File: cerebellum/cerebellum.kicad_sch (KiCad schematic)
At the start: 83 parts, among them J1 Power_IN, J10 Arm_R, J11 Light, J2 Power_Back, J3 GD_LINK, J4 GD_LINK, J5 Head, J7 Leg_L, J8 Leg_R, J9 Arm_L, Q1 AP2300, Q2 FH1404G6, Q3 FH1404G6, Q4 FH1404G6, U1 GD32F405VGHx, U2 TPS5430DDAR, U3 BMI088, U4 TCAN4550RGYRQ1, U5 ICP-20100, Y1 8M, Y2 40M

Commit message: [New] Complete new cerebellum
1. it's based on NXP MIMXRT1061CVL5A
2. it supports xt30(2+2)x7 output, xt60x1 input
3. it supports CAN FD & CAN 2.0

Signed-off-by: Homalozoa <nx.tardis@gmail.com>
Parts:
- removed J2: Power_Back, Rolling_Custom:AMASS_XT60PW-M, symbol Rolling_Custom:XT60PW-M
- removed L1: 20R, Resistor_SMD:R_0402_1005Metric, symbol Device:L_Ferrite
- removed Q2, Q3, Q4: FH1404G6, Rolling_Custom:PDFN5X6-8L, symbol Rolling_Custom:WNM6006
- removed U1: GD32F405VGHx, Rolling_Custom:Modified-BGA-100_7x7mm_Layout12x12_P0.5mm, symbol Rolling_Custom:GD32F405VGHx
- removed U4: TCAN4550RGYRQ1, Rolling_Custom:VQFN20, symbol Rolling_Custom:TCAN4550RGYRQ1
- removed Y1: 8M, Oscillator:Oscillator_SMD_EuroQuartz_XO32-4Pin_3.2x2.5mm, symbol Device:Crystal_GND24
- removed Y2: 40M, Oscillator:Oscillator_SMD_EuroQuartz_XO32-4Pin_3.2x2.5mm, symbol Device:Crystal_GND24
- added C36: 47uf 50V, Capacitor_SMD:C_0603_1608Metric, symbol Device:C
- added C38: 100nF, 10%, 10V, Capacitor_SMD:C_0402_1005Metric, symbol Device:C
- added D5: LTST-C281KFKT-5A, LED_SMD:LED_0402_1005Metric, symbol Device:LED
- added D6, D7: 12V, Diode_SMD:D_SOD-323, symbol Device:D_TVS
- added D8: B240, Diode_SMD:D_SMB, symbol Diode:B240
- added J12: Back, Rolling_Custom:XT30PW(2+2), symbol Rolling_Custom:XT30PW(2+2)
- added J2: UART, Connector_JST:JST_GH_SM03B-GHS-TB_1x03-1MP_P1.25mm_Horizontal, symbol Connector:Conn_01x03_Female
- added L1: 15uh, Inductor_SMD:L_0603_1608Metric, symbol Device:L
- added R16: 10.2k, Resistor_SMD:R_0402_1005Metric, symbol Device:R_US
- added R17: 1.96k, Resistor_SMD:R_0402_1005Metric, symbol Device:R_US
- added U1: OK1061-S, Rolling_Custom:OK1061-S-100, symbol Rolling_Custom:OK1061-S
- added U4, U6: TJA1042T, Package_SO:SOIC-8_3.9x4.9mm_P1.27mm, symbol Interface_CAN_LIN:TJA1042T
- added U7: TPS54231, Package_SO:SOIC-8_3.9x4.9mm_P1.27mm, symbol Regulator_Switching:TPS54233
- C1: value 20pF, 10%, 10V -> 100nF, 10%, 10V
- C11, C9: value 10uF, 10%, 10V -> 100pF, 10%, 10V
- C12, C8: value 100nF, 10%, 10V -> 4.7uF, 10%, 10V
- C14: value 8.2pF, 10%, 50V -> 10pf 50V
- C15: value 8.2pF, 10%, 50V -> 1.5nf 50V; footprint Capacitor_SMD:C_0402_1005Metric -> Capacitor_SMD:C_0603_1608Metric
- C16: value 10nF, 10%, 50V -> 4.7uF 50V; footprint Capacitor_SMD:C_0402_1005Metric -> Capacitor_SMD:C_0805_2012Metric
- C18: value 470nF, 10%, 50V -> 4.7uF 50V; footprint Capacitor_SMD:C_0603_1608Metric -> Capacitor_SMD:C_0805_2012Metric
- C25: value 100nF, 10%, 50V -> 10uf 50V
- C26: value 10uF, 10%, 50V -> 8.2nf 50V
- C27: value 10uF, 10%, 50V -> 100nF, 10%, 10V; footprint Capacitor_SMD:C_0603_1608Metric -> Capacitor_SMD:C_0402_1005Metric
- C3: value 20pF, 10%, 10V -> 4.7uF, 10%, 10V
- C33: value 10uF, 10%, 10V -> 47uf 50V; footprint Capacitor_SMD:C_0402_1005Metric -> Capacitor_SMD:C_0603_1608Metric
- C4: value 100nF, 10%, 10V -> 1uF, 10%, 10V
- C6: value 4.7uF, 10%, 10V -> 10uF, 10%, 10V
- C7: value 1uF, 10%, 10V -> 100nF, 10%, 10V
- D2: footprint Diode_SMD:D_SOD-523 -> Diode_SMD:D_SMC
- J3: value GD_LINK -> SWD_DBG
- J4: value GD_LINK -> SWD_DBG_PIN
- J6: value (none) -> CAN; footprint (none) -> Connector_JST:JST_GH_BM02B-GHS-TBT_1x02-1MP_P1.25mm_Vertical
- R1: value 10k, 5% -> 1k
- R2: value 10k, 5% -> 120R
- R3: value 0 -> 64.9k
- R4: value 33k -> 169k
- R5: value 3k -> 20.5
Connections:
- net ICP_SCK is gone; now on net SENSOR_SCK: U5.2 (SCL)
- net ICP_SDI is gone; now on net SENSOR_SDI: U5.4 (SDA/SDIO/SDI)
- net ICP_SDO is gone; now on net SENSOR_SDO: U5.6 (SDO/AD0)
- net MCU_OSC_IN is gone; now on net GND: C1.2
- net MCU_OSC_OUT is gone; now on net GND: C3.2
- net PWR_EXPORT is gone; now on net +24V: C34.1, C35.1, C37.1, C39.1, C41.1, J10.1 (VBUS), J11.1 (VBUS), J5.1 (VBUS), J7.1 (VBUS), J8.1 (VBUS), J9.1 (VBUS)
- net TCAN_OSC_IN is gone; now on net GND: C14.2
- net TCAN_OSC_OUT is gone; now on net GND: C15.2
- net TCAN_WAKE is gone; now on net +24V: R4.1
- net +24V: now also C16.1, C18.1, J12.1 (VBUS), U7.2 (VIN); no longer C26.1, R5.1
- net +3V3: now also R1.2; no longer C10.2, C33.1, C4.1, C5.1, C6.1, C7.1, C8.1, C9.2, J3.1 (Pin_1), R1.1
- net ACC_SCS: now also U1.46 (LPSPI1_PCS2)
- net BMI_HEAT: now also U1.72 (FLEXPWM1_PWMA2)
- net CAN_H: now also U4.7 (CANH); no longer J10.3 (CAN_H), J11.3 (CAN_H), J5.3 (CAN_H), J7.3 (CAN_H), J8.3 (CAN_H), J9.3 (CAN_H)
- net CAN_L: now also U4.6 (CANL); no longer J10.4 (CAN_L), J11.4 (CAN_L), J5.4 (CAN_L), J7.4 (CAN_L), J8.4 (CAN_L), J9.4 (CAN_L)
- net GND: now also C10.2, C11.1, C12.2, C16.2, R5.2, C36.2, C38.1, D6.2 (A2), D7.2 (A2), D8.2 (A), J2.3 (Pin_3), R17.2, U1.10 (GND), U1.25 (GND), U1.26 (GND), U1.3 (GND), U1.36 (GND), U1.4 (GND), U1.48 (BOOT_MODE0), U1.49 (BOOT_MODE1), U1.5 (GND), U1.50 (GND), U1.51 (GND), U1.52 (LCDIF_DATA06), U1.53 (LCDIF_DATA07), U1.67 (GND), U1.74 (GND), U1.75 (GND), U1.76 (GND), U1.82 (GND), U1.90 (GND), U4.2 (GND), U6.2 (GND), U7.7 (GND); no longer C1.1, C10.1, C14.1, C15.1, C16.1, C27.2, C3.1, R2.2, R3.1
- net GNDA: now also J12.2 (GND)
- net GYRO_SCS: now also U1.45 (LPSPI1_PCS3)
- net ICP_INT: now also U1.80 (GPIO3_IO00)
- net ICP_SCS: now also U1.70 (LPSPI1_PCS0)
- net SWCLK: now also U1.33 (SWCLK)
- net SWDIO: now also U1.32 (SWDIO)
- net CANFD_H: now reaches R2.1
- net CANFD_H: now also C11.2, J10.3 (CAN_H), J11.3 (CAN_H), J5.3 (CAN_H), J7.3 (CAN_H), J8.3 (CAN_H), J9.3 (CAN_H), D7.1 (A1), J12.3 (CAN_H), U6.7 (CANH)
- net BMI_SCK renamed SENSOR_SCK
- net SENSOR_SCK: now also U1.71 (LPSPI1_SCK)
- net BMI_SDI renamed SENSOR_SDI
- net SENSOR_SDI: now also U1.68 (LPSPI1_SDI)
- net BMI_SDO renamed SENSOR_SDO
- net SENSOR_SDO: now also U1.69 (LPSPI1_SDO)
- net NRST renamed +5V
- net +5V: now also C1.1, C10.1, C12.1, C3.1, C33.1, C4.1, C5.1, C6.1, C7.1, C8.1, J3.1 (Pin_1), C36.1, D8.1 (K), L1.1, R16.1, U1.1 (5V_SYS), U1.2 (5V_SYS), U4.3 (VCC), U6.3 (VCC); no longer R1.2
- net VCCOUT: no longer names the net of C27.1
- net VCCOUT: now also L1.2, U7.8 (PH)
- removed net VREF_D: C11.2, C12.2
- removed net VREF_S: C11.1, C12.1, R3.2
- new net: C15.1, R3.2
- new net: C38.2, U1.20 (POR_BUTTON)
- new net: R4.2, R5.1, U7.3 (EN)
- new net: C27.2, U7.1 (BOOT)
- new net: C26.1, U7.4 (SS)
- new net: D5.2 (A), R1.1
- new net 5V_CMP: C14.1, R3.1, U7.6 (COMP)
- new net 5V_FB: R16.2, R17.1, U7.5 (FB)
- new net CANFD_L: C9.2, D6.1 (A1), J10.4 (CAN_L), J11.4 (CAN_L), J12.4 (CAN_L), J5.4 (CAN_L), J7.4 (CAN_L), J8.4 (CAN_L), J9.4 (CAN_L), R2.2, U6.6 (CANL)
- new net CANFD_RX: U1.30 (CANFD3_RX), U6.4 (RXD)
- new net CANFD_TX: U1.35 (CANFD3_TX), U6.1 (TXD)
- new net CAN_RX: U1.14 (CAN2_RX), U4.4 (RXD)
- new net CAN_TX: U1.15 (CAN2_TX), U4.1 (TXD)
- new net LED_ORANGE: D5.1 (K), U1.47 (GPIO3_IO25)
- new net UART_RX: J2.2 (Pin_2), U1.23 (UART1_RXD)
- new net UART_TX: J2.1 (Pin_1), U1.24 (UART1_TXD)
- no-connect marks 65 -> 70
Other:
- moved on the sheet: C13, C17, C19, C20, C21, C22, C23, C24, C28, C29, C30, C31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

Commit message: [Update] Redesign PCB layout of cerebellum
1. Remove duplicated xt30(2+2) ports
2. Redesign PCB layout for new cerebellum
3. Add lines in cerebellum schematic to split different functional area.
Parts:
- removed C34, C35, C37, C39, C41: 47uf, Capacitor_SMD:CP_Elec_8x6.2, symbol Device:C_Polarized_US
- removed D2: ESD5Z3V3, Diode_SMD:D_SMC, symbol Diode:B340
- removed D8: B240, Diode_SMD:D_SMB, symbol Diode:B240
- removed J1: Power_IN, Rolling_Custom:AMASS_XT60PW-F, symbol Rolling_Custom:XT60PW-F
- removed J11: Light, Rolling_Custom:XT30PW(2+2), symbol Rolling_Custom:XT30PW(2+2)
- removed J12: Back, Rolling_Custom:XT30PW(2+2), symbol Rolling_Custom:XT30PW(2+2)
- removed J5: Head, Rolling_Custom:XT30PW(2+2), symbol Rolling_Custom:XT30PW(2+2)
- removed J7: Leg_L, Rolling_Custom:XT30PW(2+2), symbol Rolling_Custom:XT30PW(2+2)
- removed J8: Leg_R, Rolling_Custom:XT30PW(2+2), symbol Rolling_Custom:XT30PW(2+2)
- removed U2: TPS5430DDAR, Rolling_Custom:TPS5430DDAR, symbol Rolling_Custom:TPS5430DDAR
- added D2: BZT52C3V3S, Diode_SMD:D_SOD-323, symbol Diode:BZT52Bxx
- added D8: BZT52C5V1S, Diode_SMD:D_SOD-323, symbol Diode:BZT52Bxx
- added U2: TPS5430DDA, Package_SO:TI_SO-PowerPAD-8_ThermalVias, symbol Regulator_Switching:TPS5430DDA
- J1: renamed from J9; value Arm_L -> PowerIn
- J5: renamed from J10; value Arm_R -> PowerOut
- L1, L2: value 15uh -> 15uh, SLO0530H150MTT; footprint Inductor_SMD:L_0603_1608Metric -> Inductor_SMD:L_Sunlord_MWSA0518_5.4x5.2mm
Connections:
- net +24V: now also U2.7 (VIN)
- net +5V: now also D8.1 (K)
- net GND: now also D2.2 (A), D8.2 (A), U2.6 (GND), U2.9 (GNDPAD)
- net TPS_VSEN: now also U2.4 (VSENSE)
- net at C17.1: now also U2.1 (BOOT)
- net at C17.2, L2.2: now also D2.1 (K), U2.8 (PH)
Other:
- note added: "24V to 3.3V converter circuits"
- note added: "24V to 5V converter circuits"
- note added: "BMI088/055 IMU & its peripheral circuits"
- note added: "NXP MCU module's & CAN bus's peripheral circuits"
- note added: "Ports"
- note added: "Power flags"
- note added: "TDK preasure sensor & its peripheral circuits"
- moved on the sheet: C10, C12, C13, C14, C15, C16, C18, C20, C25, C26, C27, C29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

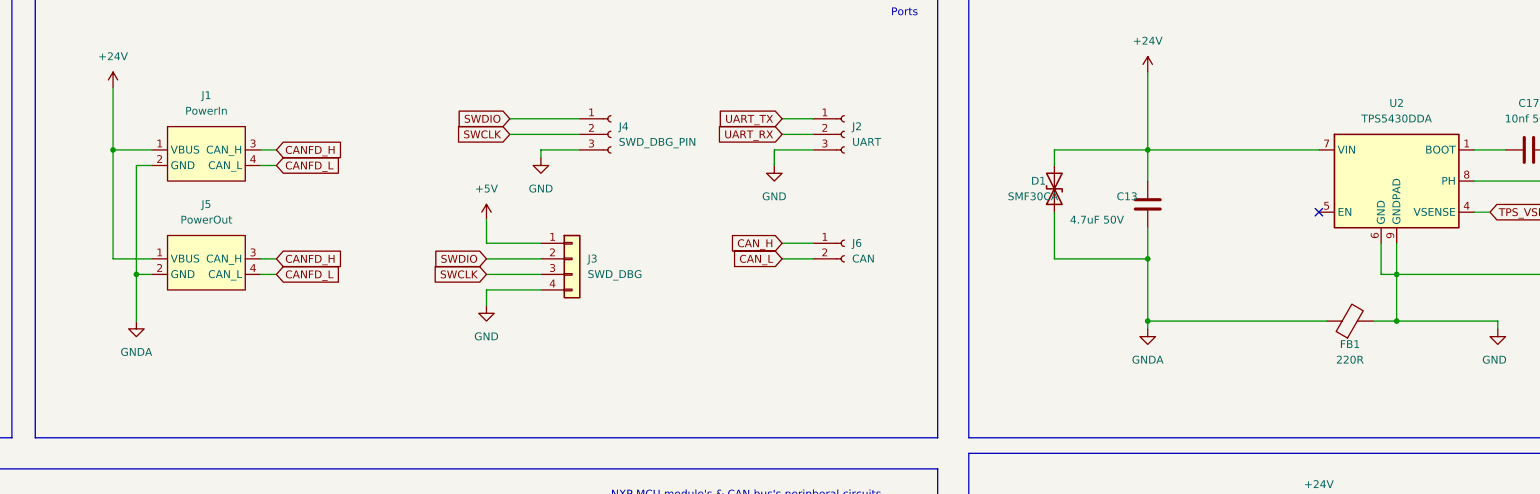
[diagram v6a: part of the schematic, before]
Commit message: [New] Rerouting cerebellum & add dxfs
1. Rerouting cerebellum for new design. There are only two layers in this design.
2. Add common board DXF file and cerebellum DXF file. Also I added their source file for convenient modification in the future.
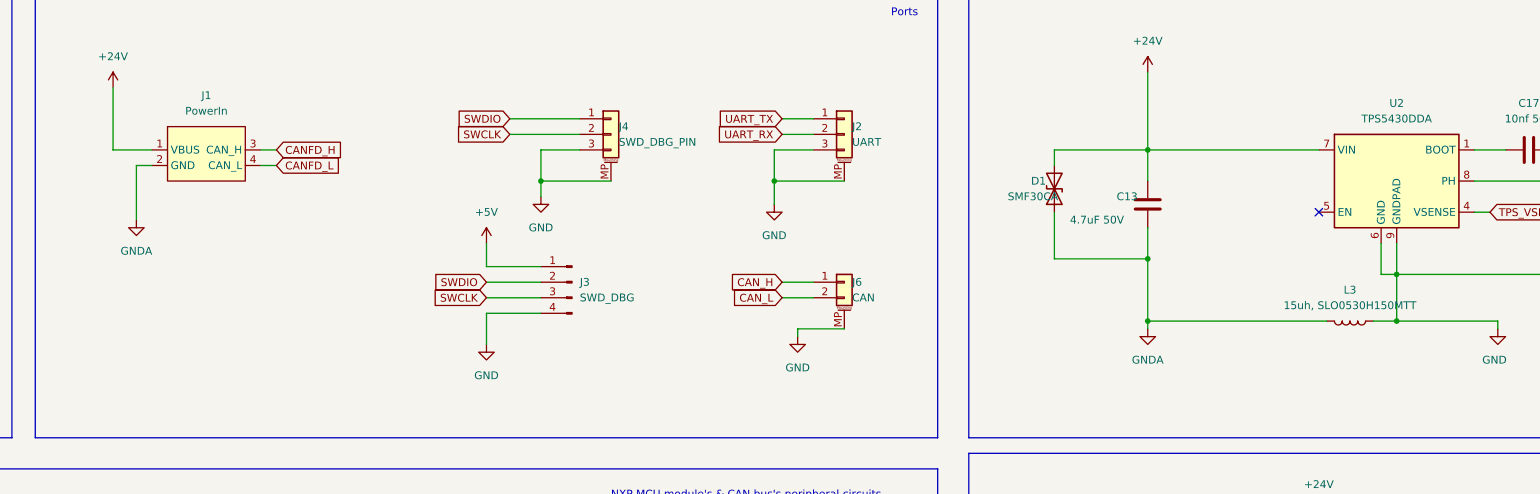
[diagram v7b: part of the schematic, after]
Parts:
- removed FB1: 220R, Resistor_SMD:R_0603_1608Metric, symbol Device:FerriteBead
- removed J5: PowerOut, Rolling_Custom:XT30PW(2+2), symbol Rolling_Custom:XT30PW(2+2)
- added L3: 15uh, SLO0530H150MTT, Inductor_SMD:L_Sunlord_MWSA0518_5.4x5.2mm, symbol Device:L
- J2, J4: symbol Connector:Conn_01x03_Female -> Connector_Generic_MountingPin:Conn_01x03_MountingPin
- J3: symbol Connector_Generic:Conn_01x04 -> Connector:Conn_01x04_Male
- J6: footprint Connector_JST:JST_GH_BM02B-GHS-TBT_1x02-1MP_P1.25mm_Vertical -> Connector_JST:JST_GH_SM02B-GHS-TB_1x02-1MP_P1.25mm_Horizontal; symbol Connector:Conn_01x02_Female -> Connector_Generic_MountingPin:Conn_01x02_MountingPin
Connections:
- net GND: now also J2.MP (MountPin), J4.MP (MountPin), J6.MP (MountPin), L3.1
- net GNDA: now also L3.2

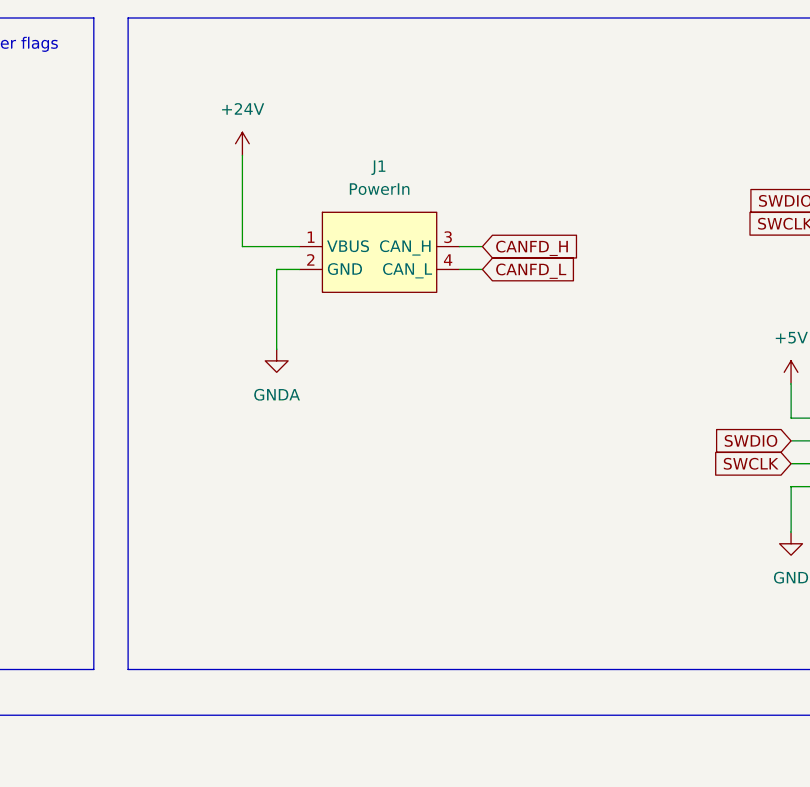
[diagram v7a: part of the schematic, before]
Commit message: [Modify] Change XT30(2+2) input to XT30 + GH 2pin
As commit before.
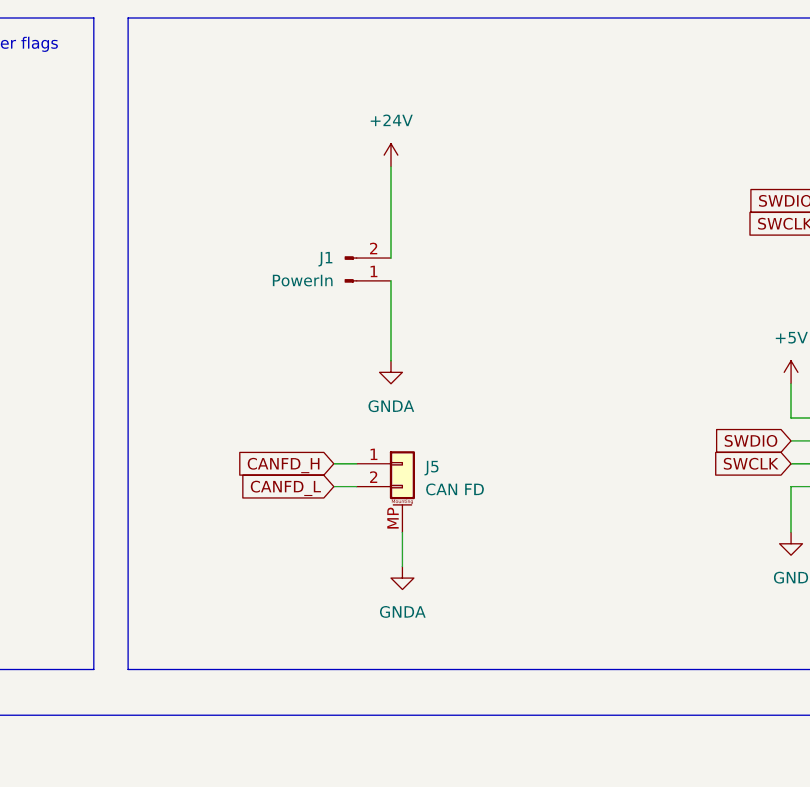
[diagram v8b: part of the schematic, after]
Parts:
- removed J1: PowerIn, Rolling_Custom:XT30PW(2+2), symbol Rolling_Custom:XT30PW(2+2)
- added J1: PowerIn, Connector_AMASS:AMASS_XT30PW-M_1x02_P2.50mm_Horizontal, symbol Connector:Conn_01x02_Male
- added J5: CAN FD, Connector_JST:JST_GH_SM02B-GHS-TB_1x02-1MP_P1.25mm_Horizontal, symbol Connector_Generic_MountingPin:Conn_01x02_MountingPin
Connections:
- net +24V: now also J1.2 (Pin_2)
- net CANFD_H: now also J5.1 (Pin_1)
- net CANFD_L: now also J5.2 (Pin_2)
- net GNDA: now also J1.1 (Pin_1), J5.MP (MountPin)
